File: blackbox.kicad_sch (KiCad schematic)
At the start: 2 parts, among them U2 W25Q128JVPIQTR

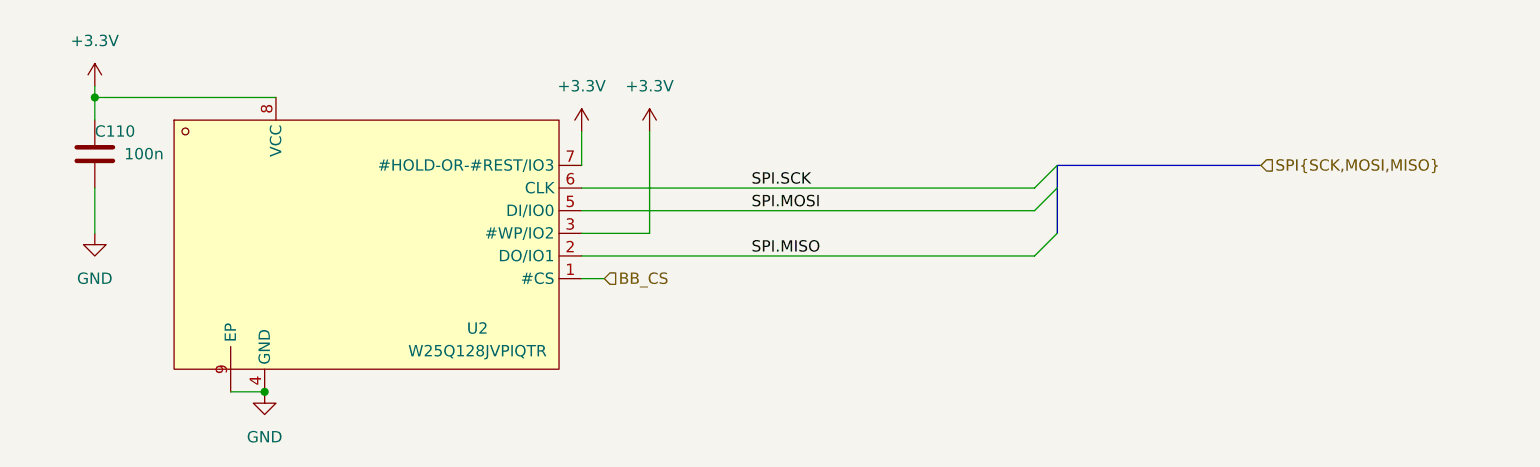
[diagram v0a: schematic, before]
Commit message: Added Open-OSD-X and new layout
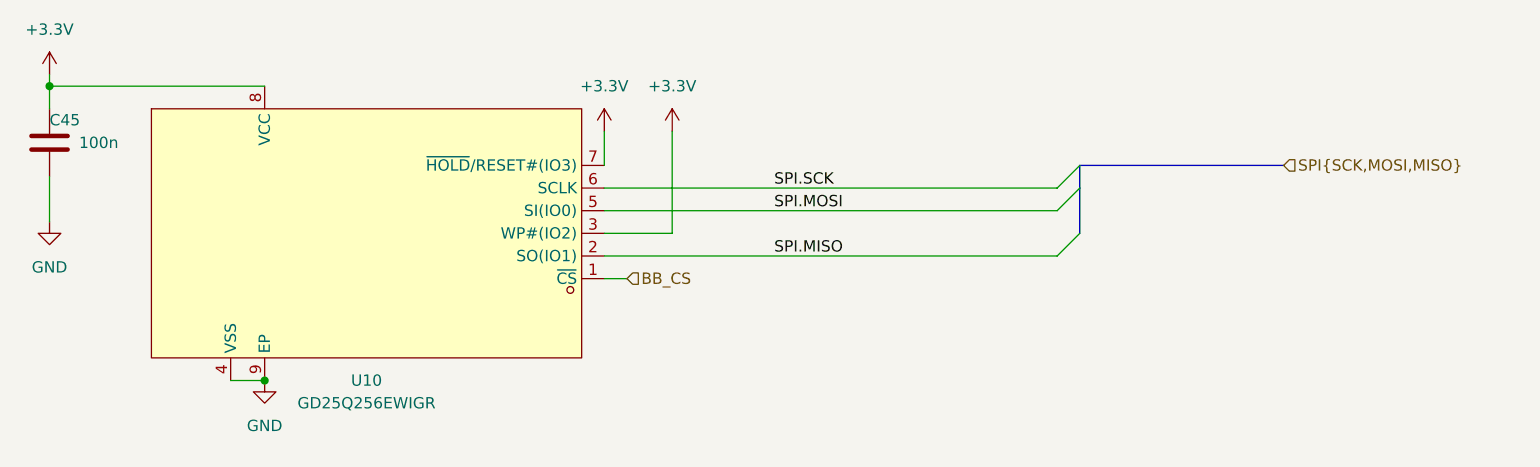
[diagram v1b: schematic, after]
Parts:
- removed C110: 100n, Capacitor_SMD:C_0402_1005Metric, symbol Device:C
- removed U2: W25Q128JVPIQTR, lib:WSON-8_L6.0-W5.0-P1.27-BL-EP, symbol lib:W25Q128JVPIQTR
- added C45: 100n, Capacitor_SMD:C_0402_1005Metric, symbol Device:C
- added U10: GD25Q256EWIGR, lib:WSON-8_L6.0-W5.0-P1.27-TL-EP, symbol lib:GD25Q256EWIGR
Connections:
- net +3.3V: now also C45.1, U10.3 (WP#(IO2)), U10.7 (~{HOLD}/RESET#(IO3)), U10.8 (VCC)
- net BB_CS: now also U10.1 (~{CS})
- net GND: now also C45.2, U10.4 (VSS), U10.9 (EP)
- net SPI.MISO: now also U10.2 (SO(IO1))
- net SPI.MOSI: now also U10.5 (SI(IO0))
- net SPI.SCK: now also U10.6 (SCLK)

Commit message: Switched to RP2354B for V2 of the FC for more IO. I want to try implement OSD on PIO state machine. I know BF already uses all of them but it should be possible and then later try to combine it witht the WS2812 protocol PIO2. If anybody here has any experience with analog OSD generation let me know, I just want to make a circuit that would allow further software development later. The reason I want to do it this way is it's cheap BOM<1 euro and low footprint, just 2 2x2 IC's and some passives.
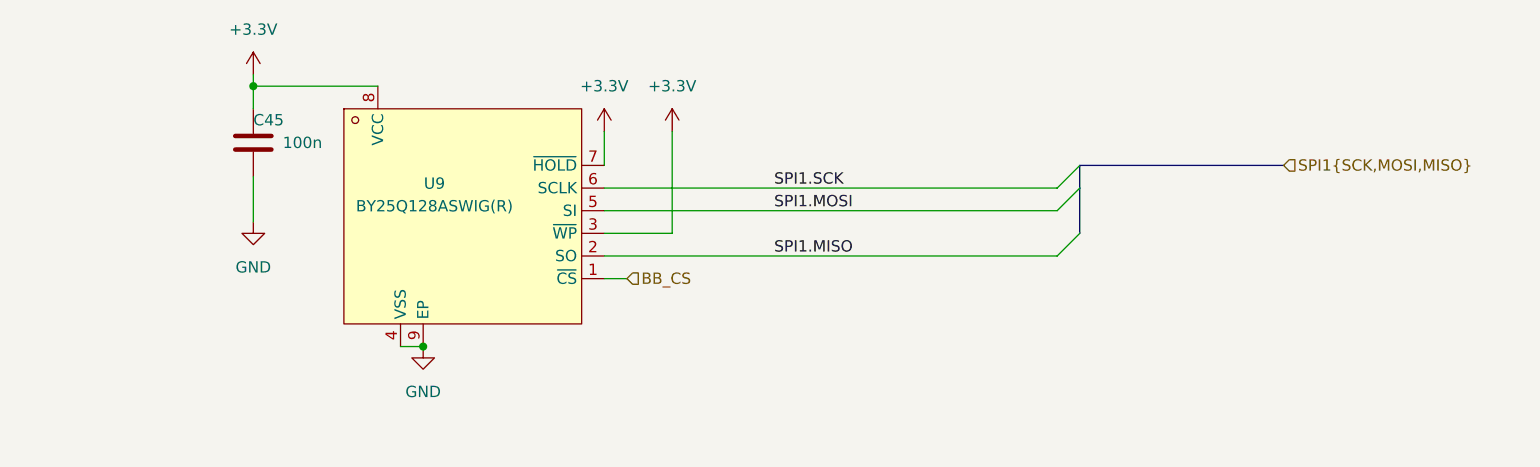
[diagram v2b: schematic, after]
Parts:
- removed U10: GD25Q256EWIGR, lib:WSON-8_L6.0-W5.0-P1.27-TL-EP, symbol lib:GD25Q256EWIGR
- added U9: BY25Q128ASWIG(R), lib:WSON-8_L6.0-W5.0-P1.27-BL-EP, symbol lib:BY25Q128ASWIG(R)
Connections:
- net +3.3V: now also U9.3 (~{WP}), U9.7 (~{HOLD}), U9.8 (VCC)
- net BB_CS: now also U9.1 (~{CS})
- net GND: now also U9.4 (VSS), U9.9 (EP)
- new net SPI1.MISO: U9.2 (SO)
- new net SPI1.MOSI: U9.5 (SI)
- new net SPI1.SCK: U9.6 (SCLK)
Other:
- moved on the sheet: C45
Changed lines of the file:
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@@
 	(paper "A5")
 	(junction
-		(at 29.21 50.8)
+		(at 52.07 50.8)
 		(diameter 0)
 		(color 0 0 0 0)
 	)
 	(junction
-		(at 53.34 83.82)
+		(at 71.12 80.01)
 		(diameter 0)
 		(color 0 0 0 0)
@@
 	(wire
 		(pts
-			(xy 29.21 49.53) (xy 29.21 50.8)
+			(xy 52.07 49.53) (xy 52.07 50.8)
 		)
 		(stroke
@@
 	(wire
 		(pts
-			(xy 29.21 50.8) (xy 53.34 50.8)
-		)
-		(stroke
-			(width 0)
-			(type default)
-		)
-	)
-	(wire
-		(pts
-			(xy 29.21 60.96) (xy 29.21 66.04)
+			(xy 52.07 50.8) (xy 66.04 50.8)
+		)
+		(stroke
+			(width 0)
+			(type default)
+		)
+	)
+	(wire
+		(pts
+			(xy 52.07 60.96) (xy 52.07 66.04)
 		)
 		(stroke
@@
 	(wire
 		(pts
+			(xy 68.58 80.01) (xy 71.12 80.01)
+		)
+		(stroke
+			(width 0)
+			(type default)
+		)
+	)
+	(wire
+		(pts
 			(xy 91.44 72.39) (xy 93.98 72.39)
 		)
@@
 	(wire
 		(pts
-			(xy 29.21 50.8) (xy 29.21 53.34)
-		)
-		(stroke
-			(width 0)
-			(type default)
-		)
-	)
-	(wire
-		(pts
-			(xy 49.53 83.82) (xy 53.34 83.82)
-		)
-		(stroke
-			(width 0)
-			(type default)
-		)
-	)
-	(label "SPI.SCK"
+			(xy 52.07 50.8) (xy 52.07 53.34)
+		)
+		(stroke
+			(width 0)
+			(type default)
+		)
+	)
+	(label "SPI1.SCK"
 		(at 110.49 62.23 0)
 		(effects
@@
 		)
 	)
-	(label "SPI.MISO"
+	(label "SPI1.MISO"
 		(at 110.49 69.85 0)
 		(effects
@@
 		)
 	)
-	(label "SPI.MOSI"
+	(label "SPI1.MOSI"
 		(at 110.49 64.77 0)
 		(effects
@@
 		)
 	)
-	(hierarchical_label "SPI{SCK,MOSI,MISO}"
+	(hierarchical_label "SPI1{SCK,MOSI,MISO}"
 		(shape input)
 		(at 167.64 59.69 0)
@@
 	)
 	(symbol
-		(lib_id "lib:GD25Q256EWIGR")
-		(at 64.77 74.93 0)
-		(unit 1)
-		(exclude_from_sim no)
-		(in_bom yes)
-		(on_board yes)
-		(dnp no)
-		(fields_autoplaced yes)
-		(property "Reference" "U10"
-			(at 64.77 83.82 0)
-			(effects
-				(font
-					(size 1.27 1.27)
-				)
-			)
-		)
-		(property "Value" "GD25Q256EWIGR"
-			(at 64.77 86.36 0)
-			(effects
-				(font
-					(size 1.27 1.27)
-				)
-			)
-		)
-		(property "Footprint" "lib:WSON-8_L6.0-W5.0-P1.27-TL-EP"
-			(at 64.77 86.36 0)
-			(effects
-				(font
-					(size 1.27 1.27)
-				)
-				(hide yes)
-			)
-		)
-		(property "Datasheet" ""
-			(at 64.77 74.93 0)
-			(effects
-				(font
-					(size 1.27 1.27)
-				)
-				(hide yes)
-			)
-		)
-		(property "Description" ""
-			(at 64.77 74.93 0)
-			(effects
-				(font
-					(size 1.27 1.27)
-				)
-				(hide yes)
-			)
-		)
-		(property "LCSC Part" "C6564321"
-			(at 64.77 88.9 0)
-			(effects
-				(font
-					(size 1.27 1.27)
-				)
-				(hide yes)
-			)
-		)
-		(pin "2"
-		)
-		(pin "3"
-		)
-		(pin "8"
-		)
-		(pin "7"
-		)
-		(pin "4"
-		)
-		(pin "9"
-		)
-		(pin "6"
-		)
-		(pin "5"
-		)
-		(pin "1"
-		)
-		(instances
-			(project ""
-				(path "/fb88b6f9-ee39-4640-a9d4-04a17ceeac64/4c4f8c63-c695-4758-b1bc-c8af53273c68"
-					(reference "U10")
-					(unit 1)
-				)
-			)
-		)
-	)
-	(symbol
 		(lib_id "power:GND")
-		(at 53.34 83.82 0)
+		(at 71.12 80.01 0)
 		(unit 1)
 		(exclude_from_sim no)
@@
 		(fields_autoplaced yes)
 		(property "Reference" "#PWR0125"
-			(at 53.34 90.17 0)
+			(at 71.12 86.36 0)
 			(effects
 				(font
@@
 		)
 		(property "Value" "GND"
-			(at 53.34 88.9 0)
+			(at 71.12 85.09 0)
 			(effects
 				(font
@@
 		)
 		(property "Footprint" ""
-			(at 53.34 83.82 0)
+			(at 71.12 80.01 0)
 			(effects
 				(font
@@
 		)
 		(property "Datasheet" ""
-			(at 53.34 83.82 0)
+			(at 71.12 80.01 0)
 			(effects
 				(font
@@
 		)
 		(property "Description" "Power symbol creates a global label with name \"GND\" , ground"
-			(at 53.34 83.82 0)
+			(at 71.12 80.01 0)
 			(effects
 				(font
@@
 	(symbol
 		(lib_id "Device:C")
-		(at 29.21 57.15 0)
+		(at 52.07 57.15 0)
 		(unit 1)
 		(exclude_from_sim no)
@@
 		(dnp no)
 		(property "Reference" "C45"
-			(at 29.21 54.61 0)
+			(at 52.07 54.61 0)
 			(effects
 				(font
@@
 		)
 		(property "Value" "100n"
-			(at 32.512 57.15 0)
+			(at 55.372 57.15 0)
 			(effects
 				(font
@@
 		)
 		(property "Footprint" "Capacitor_SMD:C_0402_1005Metric"
-			(at 30.1752 60.96 0)
+			(at 53.0352 60.96 0)
 			(effects
 				(font
@@
 		)
 		(property "Datasheet" "~"
-			(at 29.21 57.15 0)
+			(at 52.07 57.15 0)
 			(effects
 				(font
@@
 		)
 		(property "Description" ""
-			(at 29.21 57.15 0)
+			(at 52.07 57.15 0)
 			(effects
 				(font
@@
 		)
 		(property "LCSC" "C1525"
-			(at 29.21 57.15 0)
+			(at 52.07 57.15 0)
 			(effects
 				(font
@@
 	(symbol
 		(lib_id "power:GND")
-		(at 29.21 66.04 0)
+		(at 52.07 66.04 0)
 		(unit 1)
 		(exclude_from_sim no)
@@
 		(fields_autoplaced yes)
 		(property "Reference" "#PWR0124"
-			(at 29.21 72.39 0)
+			(at 52.07 72.39 0)
 			(effects
 				(font
@@
 		)
 		(property "Value" "GND"
-			(at 29.21 71.12 0)
+			(at 52.07 71.12 0)
 			(effects
 				(font
@@
 		)
 		(property "Footprint" ""
-			(at 29.21 66.04 0)
+			(at 52.07 66.04 0)
 			(effects
 				(font
@@
 		)
 		(property "Datasheet" ""
-			(at 29.21 66.04 0)
+			(at 52.07 66.04 0)
 			(effects
 				(font
@@
 		)
 		(property "Description" "Power symbol creates a global label with name \"GND\" , ground"
-			(at 29.21 66.04 0)
+			(at 52.07 66.04 0)
 			(effects
 				(font
@@
 	(symbol
 		(lib_id "power:+3.3V")
-		(at 29.21 49.53 0)
+		(at 52.07 49.53 0)
 		(unit 1)
 		(exclude_from_sim no)
@@
 		(fields_autoplaced yes)
 		(property "Reference" "#PWR0123"
-			(at 29.21 53.34 0)
+			(at 52.07 53.34 0)
 			(effects
 				(font
@@
 		)
 		(property "Value" "+3.3V"
-			(at 29.21 44.45 0)
+			(at 52.07 44.45 0)
 			(effects
 				(font
@@
 		)
 		(property "Footprint" ""
-			(at 29.21 49.53 0)
+			(at 52.07 49.53 0)
 			(effects
 				(font
@@
 		)
 		(property "Datasheet" ""
-			(at 29.21 49.53 0)
+			(at 52.07 49.53 0)
 			(effects
 				(font
@@
 		)
 		(property "Description" "Power symbol creates a global label with name \"+3.3V\""
-			(at 29.21 49.53 0)
+			(at 52.07 49.53 0)
 			(effects
 				(font
@@
 					(unit 1)
 				)
+			)
+		)
+	)
+	(symbol
+		(lib_id "lib:BY25Q128ASWIG(R)")
+		(at 71.12 60.96 0)
+		(unit 1)
+		(exclude_from_sim no)
+		(in_bom yes)
+		(on_board yes)
+		(dnp no)
+		(property "Reference" "U9"
+			(at 72.39 61.722 0)
+			(effects
+				(font
+					(size 1.27 1.27)
+				)
+			)
+		)
+		(property "Value" "BY25Q128ASWIG(R)"
+			(at 72.39 64.262 0)
+			(effects
+				(font
+					(size 1.27 1.27)
+				)
+			)
+		)
+		(property "Footprint" "lib:WSON-8_L6.0-W5.0-P1.27-BL-EP"
+			(at 71.12 73.66 0)
+			(effects
+				(font
+					(size 1.27 1.27)
+				)
+				(hide yes)
+			)
+		)
+		(property "Datasheet" ""
+			(at 71.12 60.96 0)
+			(effects
+				(font
+					(size 1.27 1.27)
+				)
+				(hide yes)
+			)
+		)
+		(property "Description" ""
+			(at 71.12 60.96 0)
+			(effects
+				(font
+					(size 1.27 1.27)
+				)
+				(hide yes)
+			)
+		)
+		(property "LCSC Part" "C394872"
+			(at 71.12 76.2 0)
+			(effects
+				(font
+					(size 1.27 1.27)
+				)
+				(hide yes)
+			)
+		)
+		(pin "5"
+		)
+		(pin "1"
+		)
+		(pin "3"
+		)
+		(pin "2"
+		)
+		(pin "4"
+		)
+		(pin "8"
+		)
+		(pin "9"
+		)
+		(pin "7"
+		)
+		(pin "6"
+		)
+		(instances
+			(project ""
+				(path "/fb88b6f9-ee39-4640-a9d4-04a17ceeac64/4c4f8c63-c695-4758-b1bc-c8af53273c68"
+					(reference "U9")
+					(unit 1)
+				)
